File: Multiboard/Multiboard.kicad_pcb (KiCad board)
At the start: 2 copper layers, 120 x 120 mm, 88 parts, among them J1 Conn_01x20_Socket, J2 Conn_01x20_Socket, J3 Debug, J4 USB_C_Receptacle_USB2.0_16P, Q1 Q_Dual_NMOS_G1S2G2D2S1D1, Q14 Q_Dual_NMOS_G1S2G2D2S1D1, Q3 Q_Dual_NMOS_G1S2G2D2S1D1, Q4 Q_Dual_NMOS_G1S2G2D2S1D1, Q5 Q_Dual_NMOS_G1S2G2D2S1D1, Q6 Q_Dual_NMOS_G1S2G2D2S1D1, Q7 Q_Dual_NMOS_G1S2G2D2S1D1, SW1 BOOT0, SW2 NRST, SW3 SW_SPST, SW4 SW_SPST, SW5 SW_SPST, SW6 SW_SPST, SW7 KEY, SW8 SW_SPST, U1 STM32F411RET6, U2 MAX662AESA_T, U3 MCP1792x-3302xCB, Y1 32.768KHz, Y2 25MHz

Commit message: Completed mcu usb-c, mcu oscillators and mcu jtag pins
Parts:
- added C20: 0.1uF, Capacitor_SMD:C_0603_1608Metric_Pad1.08x0.95mm_HandSolder, F.Cu at (263.9, 97.2)
- added C21: 10uF, Capacitor_SMD:C_0603_1608Metric_Pad1.08x0.95mm_HandSolder, F.Cu at (263.9, 99.7)
- added C22: 18pF, Capacitor_SMD:C_0603_1608Metric_Pad1.08x0.95mm_HandSolder, F.Cu at (263.9, 102.2)
- added C23: 18pF, Capacitor_SMD:C_0603_1608Metric_Pad1.08x0.95mm_HandSolder, F.Cu at (263.9, 104.8)
- added C24: 0.1uF, Capacitor_SMD:C_0603_1608Metric_Pad1.08x0.95mm_HandSolder, F.Cu at (263.9, 107.3)
- added C25: 0.1uF, Capacitor_SMD:C_0603_1608Metric_Pad1.08x0.95mm_HandSolder, F.Cu at (263.9, 109.8)
- added C26: 0.1uF, Capacitor_SMD:C_0603_1608Metric_Pad1.08x0.95mm_HandSolder, F.Cu at (263.9, 112.3)
- added C27: 0.1uF, Capacitor_SMD:C_0603_1608Metric_Pad1.08x0.95mm_HandSolder, F.Cu at (263.9, 114.8)
- added C28: 0.1uF, Capacitor_SMD:C_0603_1608Metric_Pad1.08x0.95mm_HandSolder, F.Cu at (263.9, 117.3)
- added C29: 0.1uF, Capacitor_SMD:C_0603_1608Metric_Pad1.08x0.95mm_HandSolder, F.Cu at (263.9, 119.8)
- added C30: 0.1uF, Capacitor_SMD:C_0603_1608Metric_Pad1.08x0.95mm_HandSolder, F.Cu at (268.2, 97.2)
- added C31: 4.7uF, Capacitor_SMD:C_0603_1608Metric_Pad1.08x0.95mm_HandSolder, F.Cu at (268.2, 99.7)
- added C32: 0.1uF, Capacitor_SMD:C_0603_1608Metric_Pad1.08x0.95mm_HandSolder, F.Cu at (268.2, 102.2)
- added C33: 4.7uF, Capacitor_SMD:C_0603_1608Metric_Pad1.08x0.95mm_HandSolder, F.Cu at (268.2, 104.8)
- added C34: 0.1uF, Capacitor_SMD:C_0603_1608Metric_Pad1.08x0.95mm_HandSolder, F.Cu at (226.8, 111.2)
- added C35: 0.1uF, Capacitor_SMD:C_0603_1608Metric_Pad1.08x0.95mm_HandSolder, F.Cu at (226.8, 113.7)
- added C36: 0.1uF, Capacitor_SMD:C_0603_1608Metric_Pad1.08x0.95mm_HandSolder, F.Cu at (226.8, 116.2)
- added C37: 0.1uF, Capacitor_SMD:C_0603_1608Metric_Pad1.08x0.95mm_HandSolder, F.Cu at (226.8, 118.7)
- added C38: 0.1uF, Capacitor_SMD:C_0603_1608Metric_Pad1.08x0.95mm_HandSolder, F.Cu at (226.8, 121.2)
- added C39: 0.1uF, Capacitor_SMD:C_0603_1608Metric_Pad1.08x0.95mm_HandSolder, F.Cu at (226.8, 123.8)
- added C40: 0.1uF, Capacitor_SMD:C_0603_1608Metric_Pad1.08x0.95mm_HandSolder, F.Cu at (226.8, 126.3)
- added C41: 0.1uF, Capacitor_SMD:C_0603_1608Metric_Pad1.08x0.95mm_HandSolder, F.Cu at (226.8, 128.8)
- added C42: 0.1uF, Capacitor_SMD:C_0603_1608Metric_Pad1.08x0.95mm_HandSolder, F.Cu at (226.8, 131.3)
- added C43: 0.1uF, Capacitor_SMD:C_0603_1608Metric_Pad1.08x0.95mm_HandSolder, F.Cu at (226.8, 133.8)
- added C44: 0.1uF, Capacitor_SMD:C_0603_1608Metric_Pad1.08x0.95mm_HandSolder, F.Cu at (226.8, 136.3)
- added C45: 0.1uF, Capacitor_SMD:C_0603_1608Metric_Pad1.08x0.95mm_HandSolder, F.Cu at (231.1, 111.2)
- added C46: 0.1uF, Capacitor_SMD:C_0603_1608Metric_Pad1.08x0.95mm_HandSolder, F.Cu at (231.1, 113.7)
- added C47: 0.1uF, Capacitor_SMD:C_0603_1608Metric_Pad1.08x0.95mm_HandSolder, F.Cu at (231.1, 116.2)
- added C48: 0.1uF, Capacitor_SMD:C_0603_1608Metric_Pad1.08x0.95mm_HandSolder, F.Cu at (231.1, 118.7)
- added C49: 0.1uF, Capacitor_SMD:C_0603_1608Metric_Pad1.08x0.95mm_HandSolder, F.Cu at (231.1, 121.2)
- added C50: 0.1uF, Capacitor_SMD:C_0603_1608Metric_Pad1.08x0.95mm_HandSolder, F.Cu at (231.1, 123.8)
- added C51: 0.1uF, Capacitor_SMD:C_0603_1608Metric_Pad1.08x0.95mm_HandSolder, F.Cu at (231.1, 126.3)
- added C52: 10uF, Capacitor_SMD:C_0603_1608Metric_Pad1.08x0.95mm_HandSolder, F.Cu at (231.1, 128.8)
- added C53: 22uF, Capacitor_SMD:C_0603_1608Metric_Pad1.08x0.95mm_HandSolder, F.Cu at (231.1, 131.3)
- added C54: 10uF, Capacitor_SMD:C_0603_1608Metric_Pad1.08x0.95mm_HandSolder, F.Cu at (231.1, 133.8)
- added C55: 22uF, Capacitor_SMD:C_0603_1608Metric_Pad1.08x0.95mm_HandSolder, F.Cu at (231.1, 136.3)
- added C56: 0.1uF, Capacitor_SMD:C_0603_1608Metric_Pad1.08x0.95mm_HandSolder, F.Cu at (235.5, 111.2)
- added C57: 0.1uF, Capacitor_SMD:C_0603_1608Metric_Pad1.08x0.95mm_HandSolder, F.Cu at (235.5, 113.7)
- added C58: 0.1uF, Capacitor_SMD:C_0603_1608Metric_Pad1.08x0.95mm_HandSolder, F.Cu at (235.5, 116.2)
- added C59: 0.1uF, Capacitor_SMD:C_0603_1608Metric_Pad1.08x0.95mm_HandSolder, F.Cu at (235.5, 118.7)
- added C60: 0.1uF, Capacitor_SMD:C_0603_1608Metric_Pad1.08x0.95mm_HandSolder, F.Cu at (235.5, 121.2)
- added C61: 1uF, Capacitor_SMD:C_0603_1608Metric_Pad1.08x0.95mm_HandSolder, F.Cu at (235.5, 123.8)
- added C62: 10uF, Capacitor_SMD:C_0603_1608Metric_Pad1.08x0.95mm_HandSolder, F.Cu at (235.5, 126.3)
- added C63: 0.01uF, Capacitor_SMD:C_0603_1608Metric_Pad1.08x0.95mm_HandSolder, F.Cu at (235.5, 128.8)
- added C64: 10uF, Capacitor_SMD:C_0603_1608Metric_Pad1.08x0.95mm_HandSolder, F.Cu at (235.5, 131.3)
- added C65: 1uF, Capacitor_SMD:C_0603_1608Metric_Pad1.08x0.95mm_HandSolder, F.Cu at (235.5, 133.8)
- added C66: 0.1uF, Capacitor_SMD:C_0603_1608Metric_Pad1.08x0.95mm_HandSolder, F.Cu at (235.5, 136.3)
- added C67: 0.01uF, Capacitor_SMD:C_0603_1608Metric_Pad1.08x0.95mm_HandSolder, F.Cu at (239.8, 111.2)
- added D10: GREEN, LED_SMD:LED_0603_1608Metric_Pad1.05x0.95mm_HandSolder, F.Cu at (248.6, 121.6)
- added D11: GREEN, LED_SMD:LED_0603_1608Metric_Pad1.05x0.95mm_HandSolder, F.Cu at (248.6, 124.2)
- added D12: GREEN, LED_SMD:LED_0603_1608Metric_Pad1.05x0.95mm_HandSolder, F.Cu at (248.6, 126.8)
- added D13: GREEN, LED_SMD:LED_0603_1608Metric_Pad1.05x0.95mm_HandSolder, F.Cu at (248.6, 129.4)
- added D14: GREEN, LED_SMD:LED_0603_1608Metric_Pad1.05x0.95mm_HandSolder, F.Cu at (248.6, 132.0)
- added D15: GREEN, LED_SMD:LED_0603_1608Metric_Pad1.05x0.95mm_HandSolder, F.Cu at (248.6, 134.6)
- added D16: D, Diode_SMD:D_0603_1608Metric_Pad1.05x0.95mm_HandSolder, F.Cu at (143.2, 101.2)
- added D17: D, Diode_SMD:D_0603_1608Metric_Pad1.05x0.95mm_HandSolder, F.Cu at (143.2, 97.9)
- added D18: D, Diode_SMD:D_0603_1608Metric_Pad1.05x0.95mm_HandSolder, F.Cu at (233.2, 140.1)
- added D19: D, Diode_SMD:D_0603_1608Metric_Pad1.05x0.95mm_HandSolder, F.Cu at (233.2, 142.7)
- added D6: D, Diode_SMD:D_0603_1608Metric_Pad1.05x0.95mm_HandSolder, F.Cu at (248.6, 111.2)
- added D7: GREEN, LED_SMD:LED_0603_1608Metric_Pad1.05x0.95mm_HandSolder, F.Cu at (248.6, 113.8)
- added D8: GREEN, LED_SMD:LED_0603_1608Metric_Pad1.05x0.95mm_HandSolder, F.Cu at (248.6, 116.4)
- added D9: GREEN, LED_SMD:LED_0603_1608Metric_Pad1.05x0.95mm_HandSolder, F.Cu at (248.6, 119.0)
- added J5: Conn_01x06_Socket, Connector_JST:JST_EH_S6B-EH_1x06_P2.50mm_Horizontal, F.Cu at (265.2, 93.3)
- added J6: Conn_02x20_Odd_Even, Connector_IDC:IDC-Header_2x20_P2.54mm_Vertical, F.Cu at (93.2, 79.7)
- added J7: Conn_02x20_Odd_Even, Connector_IDC:IDC-Header_2x20_P2.54mm_Vertical, F.Cu at (49.5, 138.3)
- added J8: USB_C_Receptacle_USB2.0_16P, Connector_USB:USB_C_Receptacle_G-Switch_GT-USB-7010ASV, F.Cu at (252.2, 141.2)
- added L2: 600ohm 500mA, Inductor_SMD:L_0603_1608Metric_Pad1.05x0.95mm_HandSolder, F.Cu at (268.2, 107.3)
- added L3: 600ohm 500mA, Inductor_SMD:L_0603_1608Metric_Pad1.05x0.95mm_HandSolder, F.Cu at (268.2, 109.8)
- added L4: 600ohm 500mA, Inductor_SMD:L_0603_1608Metric_Pad1.05x0.95mm_HandSolder, F.Cu at (239.8, 113.7)
- added L5: 600ohm 500mA, Inductor_SMD:L_0603_1608Metric_Pad1.05x0.95mm_HandSolder, F.Cu at (239.8, 116.2)
- added Q2: Q_Dual_NMOS_G1S2G2D2S1D1, Package_TO_SOT_SMD:SOT-23-6_Handsoldering, F.Cu at (269.0, 125.5)
- added R36: 10k, Resistor_SMD:R_0603_1608Metric_Pad0.98x0.95mm_HandSolder, F.Cu at (263.9, 124.3)
- added R37: 10k, Resistor_SMD:R_0603_1608Metric_Pad0.98x0.95mm_HandSolder, F.Cu at (263.9, 126.8)
- added R38: 10k, Resistor_SMD:R_0603_1608Metric_Pad0.98x0.95mm_HandSolder, F.Cu at (263.9, 129.3)
- added R39: 10k, Resistor_SMD:R_0603_1608Metric_Pad0.98x0.95mm_HandSolder, F.Cu at (263.9, 131.9)
- added R40: 5.1K, Resistor_SMD:R_0603_1608Metric_Pad0.98x0.95mm_HandSolder, F.Cu at (268.2, 112.3)
- added R41: 5.1K, Resistor_SMD:R_0603_1608Metric_Pad0.98x0.95mm_HandSolder, F.Cu at (268.2, 114.8)
- added R42: 5.1K, Resistor_SMD:R_0603_1608Metric_Pad0.98x0.95mm_HandSolder, F.Cu at (268.2, 117.3)
- added R43: 2.2K, Resistor_SMD:R_0603_1608Metric_Pad0.98x0.95mm_HandSolder, F.Cu at (268.2, 119.8)
- added R44: 0, Resistor_SMD:R_0603_1608Metric_Pad0.98x0.95mm_HandSolder, F.Cu at (272.6, 97.2)
- added R45: 0, Resistor_SMD:R_0603_1608Metric_Pad0.98x0.95mm_HandSolder, F.Cu at (272.6, 99.7)
- added R46: 0, Resistor_SMD:R_0603_1608Metric_Pad0.98x0.95mm_HandSolder, F.Cu at (272.6, 102.2)
- added R47: 0, Resistor_SMD:R_0603_1608Metric_Pad0.98x0.95mm_HandSolder, F.Cu at (272.6, 104.8)
- added R48: 2.2K, Resistor_SMD:R_0603_1608Metric_Pad0.98x0.95mm_HandSolder, F.Cu at (272.6, 107.3)
- added R49: 12K 1%, Resistor_SMD:R_0603_1608Metric_Pad0.98x0.95mm_HandSolder, F.Cu at (272.6, 109.8)
- added R50: 10K, Resistor_SMD:R_0603_1608Metric_Pad0.98x0.95mm_HandSolder, F.Cu at (272.6, 112.3)
- added R51: 10K, Resistor_SMD:R_0603_1608Metric_Pad0.98x0.95mm_HandSolder, F.Cu at (272.6, 114.8)
- added R52: 10K, Resistor_SMD:R_0603_1608Metric_Pad0.98x0.95mm_HandSolder, F.Cu at (272.6, 117.3)
- added R53: 0, Resistor_SMD:R_0603_1608Metric_Pad0.98x0.95mm_HandSolder, F.Cu at (272.6, 119.8)
- added R54: 0, Resistor_SMD:R_0603_1608Metric_Pad0.98x0.95mm_HandSolder, F.Cu at (276.9, 97.2)
- added R55: 0, Resistor_SMD:R_0603_1608Metric_Pad0.98x0.95mm_HandSolder, F.Cu at (276.9, 99.7)
- added R56: 0, Resistor_SMD:R_0603_1608Metric_Pad0.98x0.95mm_HandSolder, F.Cu at (276.9, 102.2)
- added R57: 0, Resistor_SMD:R_0603_1608Metric_Pad0.98x0.95mm_HandSolder, F.Cu at (276.9, 104.8)
- added R58: 2.2K, Resistor_SMD:R_0603_1608Metric_Pad0.98x0.95mm_HandSolder, F.Cu at (276.9, 107.3)
- added R59: 0, Resistor_SMD:R_0603_1608Metric_Pad0.98x0.95mm_HandSolder, F.Cu at (276.9, 109.8)
- added R60: 0, Resistor_SMD:R_0603_1608Metric_Pad0.98x0.95mm_HandSolder, F.Cu at (276.9, 112.3)
- added R61: 2.2K, Resistor_SMD:R_0603_1608Metric_Pad0.98x0.95mm_HandSolder, F.Cu at (239.8, 118.7)
- added R62: 2.2K, Resistor_SMD:R_0603_1608Metric_Pad0.98x0.95mm_HandSolder, F.Cu at (239.8, 121.2)
- added R63: 5.1K, Resistor_SMD:R_0603_1608Metric_Pad0.98x0.95mm_HandSolder, F.Cu at (239.8, 123.8)
- added R64: 5.1K, Resistor_SMD:R_0603_1608Metric_Pad0.98x0.95mm_HandSolder, F.Cu at (239.8, 126.3)
- added R65: 100, Resistor_SMD:R_0603_1608Metric_Pad0.98x0.95mm_HandSolder, F.Cu at (239.8, 128.8)
- added R66: 0, Resistor_SMD:R_0603_1608Metric_Pad0.98x0.95mm_HandSolder, F.Cu at (239.8, 131.3)
- added R67: 1K, Resistor_SMD:R_0603_1608Metric_Pad0.98x0.95mm_HandSolder, F.Cu at (239.8, 133.8)
- added R68: 0, Resistor_SMD:R_0603_1608Metric_Pad0.98x0.95mm_HandSolder, F.Cu at (239.8, 136.3)
- added R69: 1K, Resistor_SMD:R_0603_1608Metric_Pad0.98x0.95mm_HandSolder, F.Cu at (244.2, 111.2)
- added R70: 1K, Resistor_SMD:R_0603_1608Metric_Pad0.98x0.95mm_HandSolder, F.Cu at (244.2, 113.7)
- added R71: 1K, Resistor_SMD:R_0603_1608Metric_Pad0.98x0.95mm_HandSolder, F.Cu at (244.2, 116.2)
- added R72: 1K, Resistor_SMD:R_0603_1608Metric_Pad0.98x0.95mm_HandSolder, F.Cu at (244.2, 118.7)
- added R73: 1K, Resistor_SMD:R_0603_1608Metric_Pad0.98x0.95mm_HandSolder, F.Cu at (244.2, 121.2)
- added R74: 1K, Resistor_SMD:R_0603_1608Metric_Pad0.98x0.95mm_HandSolder, F.Cu at (244.2, 123.8)
- added R75: 1K, Resistor_SMD:R_0603_1608Metric_Pad0.98x0.95mm_HandSolder, F.Cu at (244.2, 126.3)
- added R76: 1K, Resistor_SMD:R_0603_1608Metric_Pad0.98x0.95mm_HandSolder, F.Cu at (244.2, 128.8)
- added U4: FT2232HL-REEL, FT2232HL:QFP50P1200X1200X160-64N, F.Cu at (88.5, 112.3)
- added U5: 93LCxxC, Package_SO:SO-8_3.9x4.9mm_P1.27mm, F.Cu at (283.3, 113.8)
- added U6: LCMXO2-1200ZE-1TG144C, LCMXO2-1200ZE-1TG144C:QFP50P2200X2200X160-144N, F.Cu at (66.3, 109.3)
- added U7: FAN1112, Package_TO_SOT_SMD:SOT-223, F.Cu at (254.8, 89.8)
- added U8: NCP1117, Package_TO_SOT_SMD:SOT-223, F.Cu at (254.8, 98.1)
- added Y3: 12MHz, Crystal:Crystal_SMD_TXC_7A-2Pin_5x3.2mm, F.Cu at (284.7, 88.0)
- Y2: footprint Crystal:Crystal_SMD_HC49-SD -> Crystal:Crystal_SMD_3225-4Pin_3.2x2.5mm
- moved J3 38.8 mm to (132.0, 86.0)
- moved C2 30.2 mm to (104.8, 90.2), turned to -90 degrees
- moved Y1 27.3 mm to (104.8, 93.9)
- moved C3 25.3 mm to (104.8, 97.7), turned to 90 degrees
- moved C4 12.9 mm to (108.1, 96.2), turned to 180 degrees
- moved C5 12.5 mm to (108.1, 102.2), turned to 0 degrees
- moved Y2 8.41 mm to (108.1, 99.2)
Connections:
- net /D+ renamed /MCU/D+
- net /D- renamed /MCU/D-
- net /PA8 renamed /MCU/PA8
- net /PB0 renamed /MCU/PB0
- net /PB1 renamed /MCU/PB1
- net /PB10 renamed /MCU/PB10
- net /PB12 renamed /MCU/PB12
- net /PB13 renamed /MCU/PB13
- net /PB14 renamed /MCU/PB14
- net /PB15 renamed /MCU/PB15
- net /PB3 renamed /MCU/PB3
- net /PB4 renamed /MCU/PB4
- net /PB5 renamed /MCU/PB5
- net /PB8 renamed /MCU/PB8
- net /PB9 renamed /MCU/PB9
- net /PC10 renamed /MCU/PC10
- net /PC11 renamed /MCU/PC11
- net /PC13 renamed /MCU/PC13
- net /SWCLK_PA14 renamed /MCU/SWCLK_PA14
- net /SWDIO_PA13 renamed /MCU/SWDIO_PA13
- net /VB renamed /MCU/VB
- C14 pad 1: /VREF+ -> GND
- C14 pad 2: GND -> Net-(C14-Pad2)
- L1 pad 2: /VREF+ -> Net-(C14-Pad2)
- Q1 pad 2: PA10-MCU -> PA5-MCU
- Q1 pad 4: PA10-GPIO -> PA5-GPIO
- Q1 pad 5: PA9-MCU -> PA4-MCU
- Q1 pad 6: PA9-GPIO -> PA4-GPIO
- Q3 pad 2: PA5-MCU -> PA10-MCU
- Q3 pad 4: PA5-GPIO -> PA10-GPIO
- Q3 pad 5: PA4-MCU -> PA9-MCU
- Q3 pad 6: PA4-GPIO -> PA9-GPIO
- Q4 pad 2: PA7-MCU -> PA1-MCU
- Q4 pad 4: PA7-GPIO -> PA1-GPIO
- Q4 pad 5: PA6-MCU -> PA0-MCU
- Q4 pad 6: PA6-GPIO -> PA0-GPIO
- R11 pad 2: Net-(SW5-B) -> Net-(SW3-B)
- R12 pad 1: PB7-MCU -> PA4-MCU
- R13 pad 1: PB7-GPIO -> PA4-GPIO
- R13 pad 2: Net-(SW3-B) -> Net-(SW4-B)
- R14 pad 1: PB6-MCU -> PA5-MCU
- R15 pad 1: PB6-GPIO -> PA5-GPIO
- R15 pad 2: Net-(SW3-B) -> Net-(SW4-B)
- R16 pad 1: PA4-MCU -> PA6-MCU
- R17 pad 1: PA4-GPIO -> PA6-GPIO
- R18 pad 1: PA5-MCU -> PA7-MCU
- R19 pad 1: PA5-GPIO -> PA7-GPIO
- R20 pad 1: PA6-MCU -> PB6-MCU
- R21 pad 1: PA6-GPIO -> PB6-GPIO
- R21 pad 2: Net-(SW4-B) -> Net-(SW5-B)
- R22 pad 1: PA7-MCU -> PB7-MCU
- R23 pad 1: PA7-GPIO -> PB7-GPIO
- R23 pad 2: Net-(SW4-B) -> Net-(SW5-B)
- R29 pad 2: Net-(SW6-B) -> Net-(SW8-B)
- R31 pad 2: Net-(SW6-B) -> Net-(SW8-B)
- R33 pad 2: Net-(SW6-B) -> Net-(SW8-B)
- R35 pad 2: Net-(SW6-B) -> Net-(SW8-B)
- R9 pad 2: Net-(SW5-B) -> Net-(SW3-B)
- Y2 pad 2: Net-(U1-PH0-OSC_IN) -> (no net)
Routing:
- net /MCU/PB3: track 0.00 -> 67.0 mm, vias 0 -> 1
- net /MCU/PB4: track 0.00 -> 66.4 mm, vias 0 -> 1
- net /MCU/PB9: track 0.00 -> 64.5 mm, vias 0 -> 2
- net /MCU/SWDIO_PA13: track 0.00 -> 17.0 mm, vias 0 -> 1
- net /MCU/SWCLK_PA14: track 0.00 -> 14.4 mm, vias 0 -> 1
- net Net-(U1-PC14-OSC32_IN): track 2.17 -> 14.3 mm
- net Net-(U1-PC15-OSC32_OUT): track 2.17 -> 14.2 mm
- net /MCU/PA8: track 49.9 -> 59.2 mm, vias 0 -> 1
- net Net-(U1-PH0-OSC_IN): track 3.70 -> 11.7 mm
- net Net-(U1-PH1-OSC_OUT): track 3.70 -> 10.2 mm
- net GND: track 89.5 -> 94.9 mm, vias 35 -> 37
- net 3V3: track 94.0 -> 97.5 mm, vias 38 -> 39
- net /MCU/D+: track 26.8 -> 30.2 mm
- net /VREF+: track 3.33 -> 0.00 mm, vias 1 -> 0
- net Net-(J1-Pin_6): track 72.1 -> 74.6 mm
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
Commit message: positioned fpga-usb
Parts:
- removed J5: Conn_01x06_Socket, Connector_JST:JST_EH_S6B-EH_1x06_P2.50mm_Horizontal
- moved J8 189.1 mm to (68.2, 97.8), turned to -90 degrees
- moved D6 174.3 mm to (75.1, 94.6), turned to -90 degrees
- moved D18 167.4 mm to (77.5, 78.7)
- moved D19 167.4 mm to (77.5, 81.3)
- moved C20 167.2 mm to (431.1, 99.8)
- moved C21 167.2 mm to (431.1, 102.3)
- moved C22 167.2 mm to (431.1, 104.8)
- moved C23 167.2 mm to (431.1, 107.3)
- moved C24 167.2 mm to (431.1, 109.8)
- moved C25 167.2 mm to (431.1, 112.3)
- moved C26 167.2 mm to (431.1, 114.9)
- moved C27 167.2 mm to (431.1, 117.4)
- moved C28 167.2 mm to (431.1, 119.9)
- moved C29 167.2 mm to (431.1, 122.4)
- moved C34 167.2 mm to (394.0, 113.8)
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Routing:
- net Net-(J2-Pin_3): track 0.00 -> 74.4 mm, vias 0 -> 2
- net /MCU/PB8: track 0.00 -> 65.7 mm, vias 0 -> 2
- net Net-(D6-A): track 0.00 -> 9.98 mm
- net Net-(J8-CC1): track 0.00 -> 5.75 mm
- net Net-(J8-CC2): track 0.00 -> 4.68 mm
- net 5V: track 83.6 -> 86.2 mm, vias 3 -> 4
- net GND: track 94.9 -> 97.4 mm, vias 37 -> 39
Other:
- board size 120 x 120 mm -> 150 x 120 mm

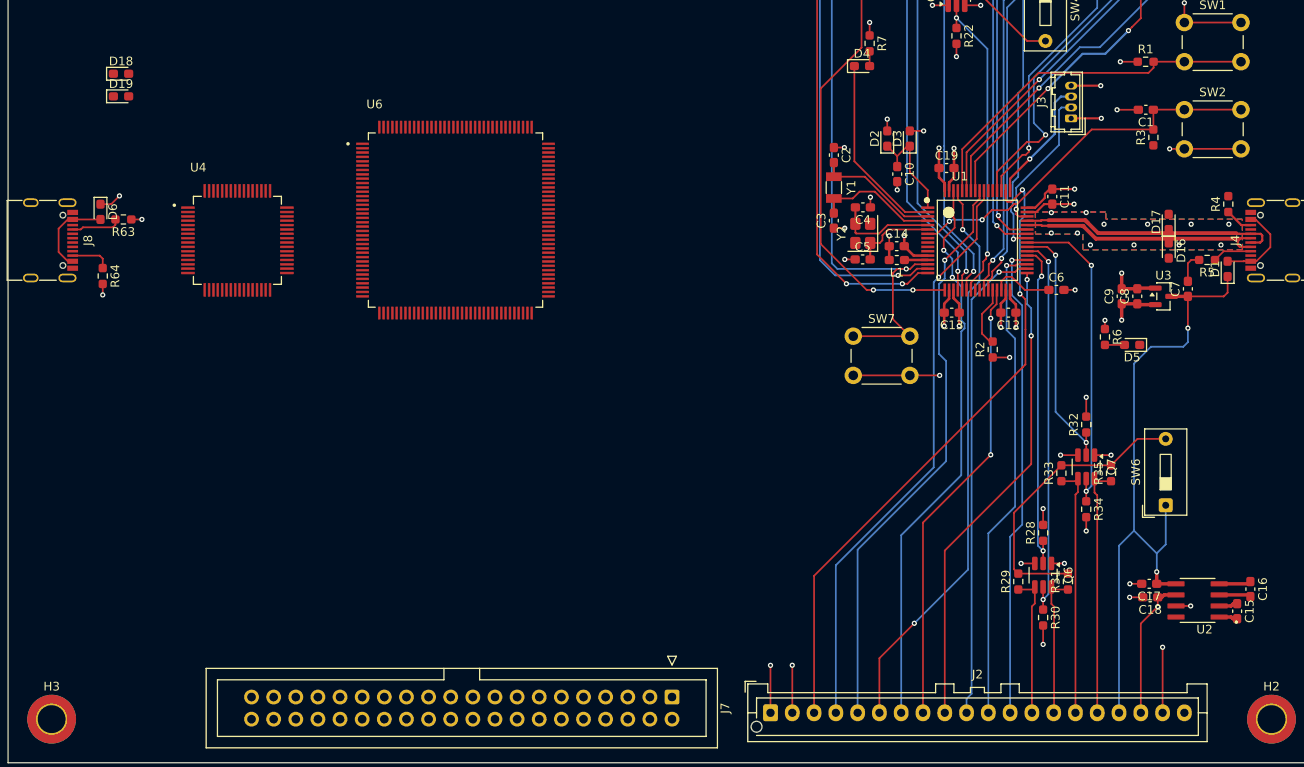
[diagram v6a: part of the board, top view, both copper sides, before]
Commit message: wired fpga usb
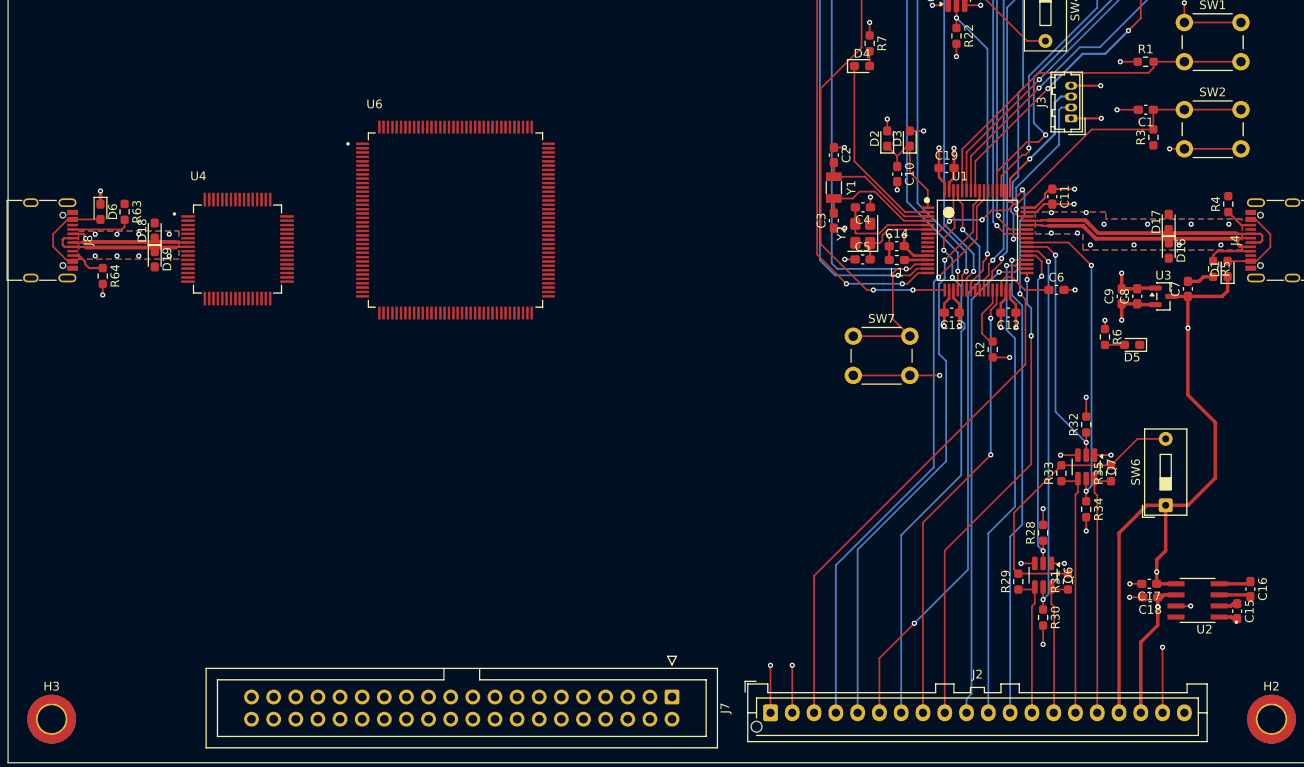
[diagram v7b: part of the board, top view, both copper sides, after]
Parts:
- moved D19 19.1 mm to (81.3, 100.0), turned to -90 degrees
- moved D18 18.4 mm to (81.3, 96.7), turned to 90 degrees
- moved R5 1.24 mm to (202.8, 101.1), turned to -90 degrees
- moved U4 1.00 mm to (90.8, 98.8)
- moved R63 0.89 mm to (77.9, 94.6), turned to -90 degrees
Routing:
- net FPGA_D+: track 0.00 -> 16.4 mm
- net FPGA_D-: track 0.00 -> 15.7 mm
- net 5V: track 86.2 -> 84.5 mm
- net GND: track 97.4 -> 95.7 mm, vias 39 -> 46
- net Net-(J8-CC1): track 5.75 -> 6.89 mm
- net Net-(J4-CC1): track 4.51 -> 5.15 mm
- net Net-(D6-A): track 9.98 -> 10.5 mm

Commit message: positioned and wired FTDI
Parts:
- added BT1: Battery_Cell, Battery:Battery_Panasonic_CR2032-VS1N_Vertical_CircularHoles, F.Cu at (173.7, 78.9)
- added J5: Conn_01x06_Socket, Connector_JST:JST_EH_S6B-EH_1x06_P2.50mm_Horizontal, F.Cu at (347.5, 128.1)
- J6, J7: footprint Connector_IDC:IDC-Header_2x20_P2.54mm_Vertical -> Connector_IDC:IDC-Header_2x20_P2.54mm_Latch_Vertical
- moved Y3 370.2 mm to (81.7, 93.9), turned to -90 degrees
- moved U5 365.2 mm to (87.5, 76.4), turned to 90 degrees
- moved R50 358.2 mm to (83.6, 76.2), turned to 90 degrees
- moved R58 355.8 mm to (89.4, 82.0), turned to 90 degrees
- moved R51 355.5 mm to (86.0, 82.9)
- moved R48 353.9 mm to (85.8, 106.6)
- moved C30 353.7 mm to (81.7, 103.4)
- moved C31 353.7 mm to (81.7, 105.9)
- moved L2 353.7 mm to (81.7, 107.7), turned to 180 degrees
- moved R49 353.3 mm to (87.4, 86.7), turned to -90 degrees
- moved C23 352.2 mm to (79.1, 92.6), turned to 90 degrees
- moved L3 351.8 mm to (84.6, 86.5), turned to 180 degrees
- moved C33 351.3 mm to (84.6, 90.0)
- moved C22 351.2 mm to (80.1, 90.0)
- moved C32 351.2 mm to (84.6, 88.3)
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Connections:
- D2 pad 2: /MCU/VB -> Net-(BT1-+)
- J2 pad 20: /MCU/VB -> 3V3
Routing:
- net GND: track 95.7 -> 144.3 mm, vias 46 -> 60
- net 3V3: track 97.5 -> 133.1 mm, vias 39 -> 45
- net Net-(U4-EECLK): track 0.00 -> 16.7 mm, vias 0 -> 2
- net Net-(U4-EEDATA): track 0.00 -> 16.7 mm, vias 0 -> 2
- net Net-(U4-VPLL): track 0.00 -> 16.4 mm
- net Net-(U4-EECS): track 0.00 -> 15.3 mm, vias 0 -> 2
- net Net-(U4-REF): track 0.00 -> 13.2 mm
- net Net-(BT1-+): track 0.00 -> 11.9 mm
- net Net-(SW5-B): track 11.7 -> 0.00 mm
- net Net-(U4-VPHY): track 0.00 -> 11.6 mm
- net Net-(U4-OSCI): track 0.00 -> 8.32 mm
- net Net-(SW8-B): track 13.8 -> 5.71 mm
- net Net-(U4-OSCO): track 0.00 -> 8.08 mm
- net Net-(SW3-B): track 14.0 -> 6.08 mm
- net Net-(U4-~{RESET}): track 0.00 -> 7.41 mm, vias 0 -> 2
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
